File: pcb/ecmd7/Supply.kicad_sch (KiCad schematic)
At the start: 28 parts, among them Q7 BSC098N10NS5, Q8 BSC098N10NS5, U3 LM5118MH

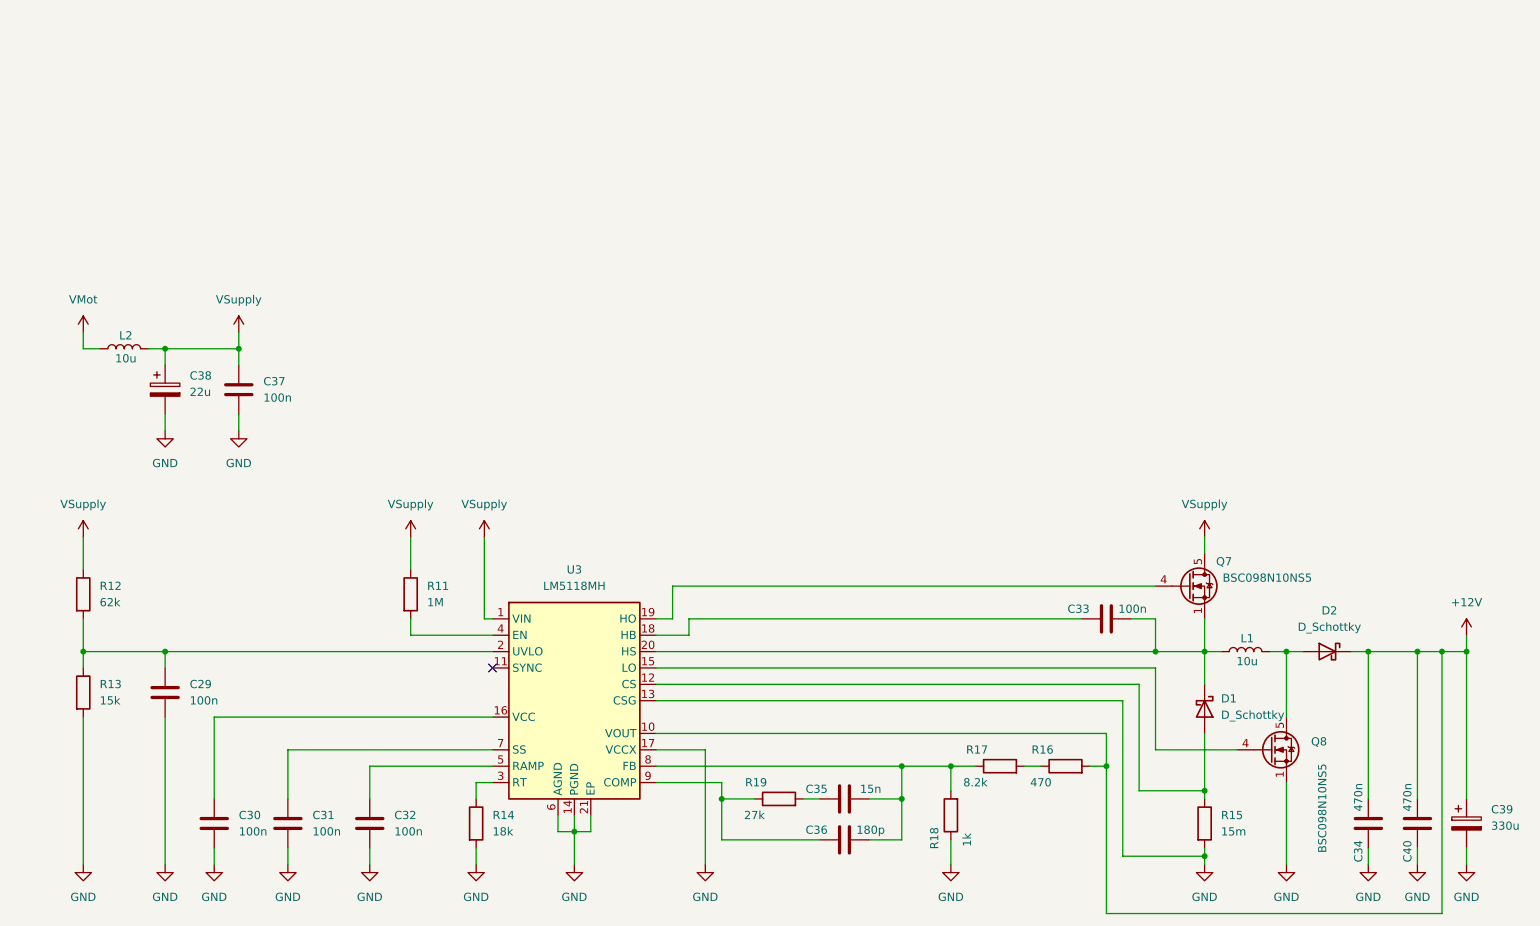
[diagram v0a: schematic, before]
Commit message: WIP: Add ADC inputs
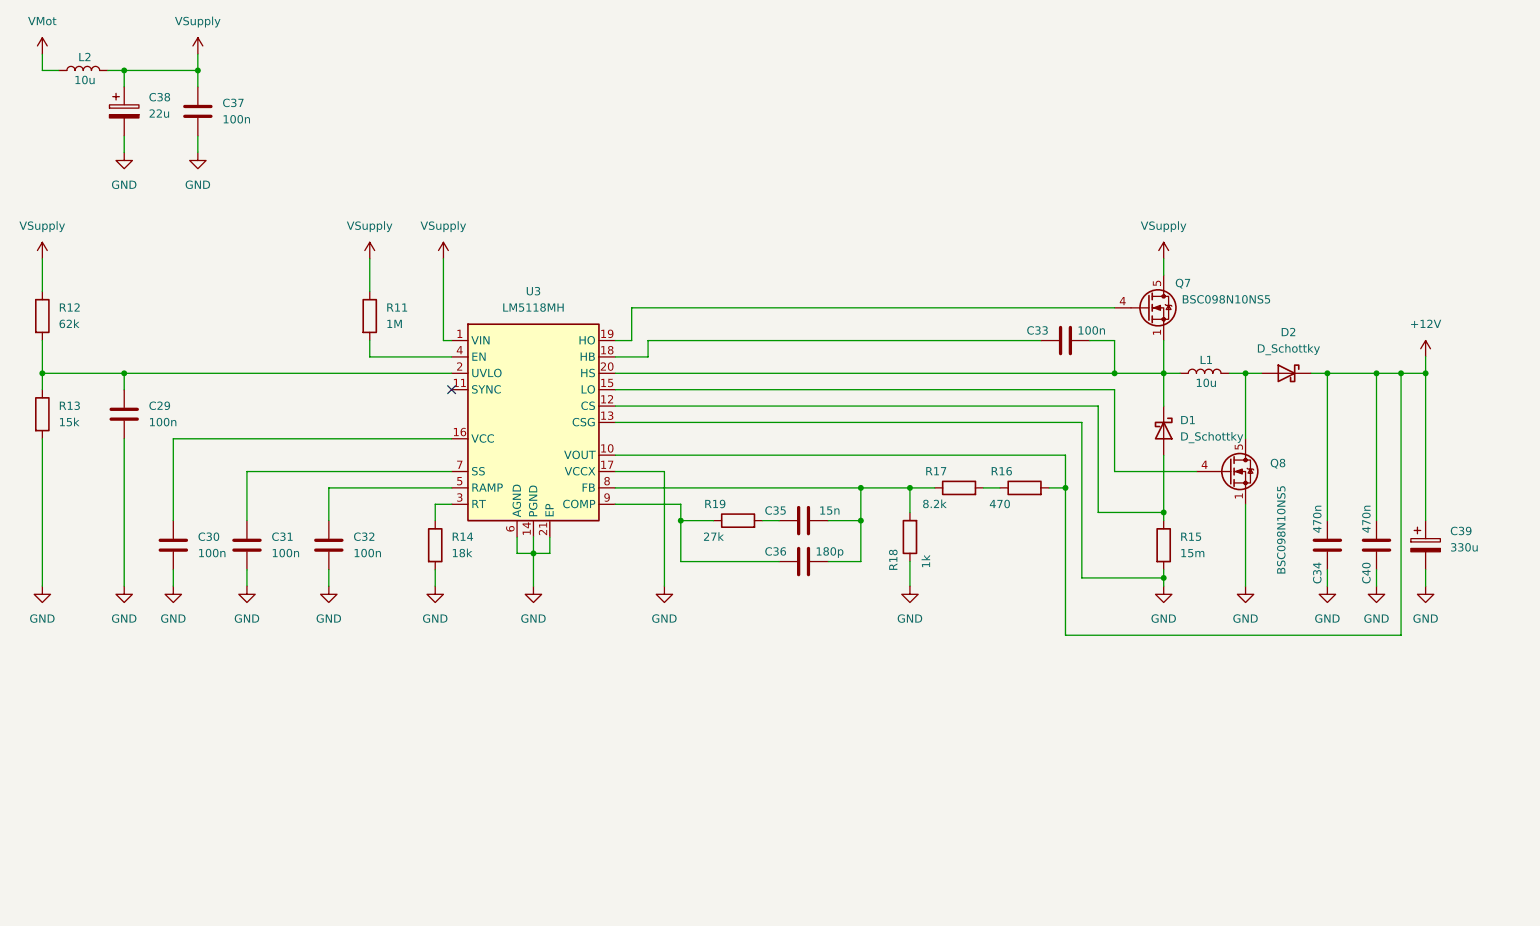
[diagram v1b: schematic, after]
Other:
- moved on the sheet: C29, C30, C31, C32, C33, C34, C35, C36, C37, C38, C39, C40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
